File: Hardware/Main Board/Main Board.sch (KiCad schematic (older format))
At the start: 48 parts, among them Q1 NPN, Q2 NPN, Q3 A04484, SW1 Momentary, U1 MT3608, U2 NCP718A, U3 ATtiny814-SS

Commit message: added footprints to schematic. Some still need to be made but mostly all are done
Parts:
- removed MK1: MIC, symbol Device:Microphone
- added C7: .1uf, Capacitor_SMD:C_0603_1608Metric, symbol Device:C_Small
- added TP10: B-, TestPoint:TestPoint_THTPad_3.0x3.0mm_Drill1.5mm, symbol Connector:TestPoint
- added TP11: Battery-, TestPoint:TestPoint_Pad_3.0x3.0mm, symbol Connector:TestPoint
- added TP12: P+, TestPoint:TestPoint_THTPad_3.0x3.0mm_Drill1.5mm, symbol Connector:TestPoint
- added TP13: P-, TestPoint:TestPoint_THTPad_3.0x3.0mm_Drill1.5mm, symbol Connector:TestPoint
- added TP14: MIC+, TestPoint:TestPoint_Keystone_5019_Minature, symbol Connector:TestPoint
- added TP15: MIC-, TestPoint:TestPoint_Keystone_5019_Minature, symbol Connector:TestPoint
- added TP6: 3V, TestPoint:TestPoint_Pad_D2.0mm, symbol Connector:TestPoint
- added TP7: Battery+, TestPoint:TestPoint_Pad_3.0x3.0mm, symbol Connector:TestPoint
- added TP8: MIC, TestPoint:TestPoint_Pad_D2.0mm, symbol Connector:TestPoint
- added TP9: B+, TestPoint:TestPoint_THTPad_3.0x3.0mm_Drill1.5mm, symbol Connector:TestPoint
- C1, C2, C3, C5, C6: footprint (none) -> Capacitor_SMD:C_Elec_4x5.4
- C10, C11, C12, C4, C8, C9: footprint (none) -> Capacitor_SMD:C_0603_1608Metric
- D1, D2, D3: footprint (none) -> Diode_SMD:D_SOD-323
- FB1: value ? -> ACML-0805-190-T; footprint (none) -> Resistor_SMD:R_0805_2012Metric
- L1: footprint (none) -> Inductor_SMD:L_Abracon_ASPI-3012S
- L2: footprint (none) -> Inductor_SMD:L_0805_2012Metric
- Q1, Q2: value NPN -> MMBT3904-TP; footprint (none) -> Package_TO_SOT_SMD:SOT-23
- R1, R12, R13, R14, R15, R16, R17, R18, R19, R2, R20, R3, R4, R5, R6, R7, R8: footprint (none) -> Resistor_SMD:R_0603_1608Metric
- SW1: footprint (none) -> Footprints:tactile
- TH1: footprint (none) -> Capacitor_SMD:C_0805_2012Metric
- TP1, TP2: footprint (none) -> TestPoint:TestPoint_Pad_3.0x3.0mm
- TP3, TP5: footprint (none) -> TestPoint:TestPoint_Pad_D2.5mm
- TP4: footprint (none) -> TestPoint:TestPoint_Pad_D2.5m
- U1: footprint (none) -> Package_TO_SOT_SMD:SOT-23-6
- U3: value ATtiny814-SS -> ATtiny1614; symbol MCU_Microchip_ATtiny:ATtiny814-SS -> Main-Board-rescue:ATtiny814-SS-MCU_Microchip_ATtiny
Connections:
- net labels added: +3.3V, GNDREF
- net labels removed: Pack_Sense, Temp_Sense
- wire segments 116 -> 134
- no-connect marks 1 -> 6
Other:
- note added: "Battery into PCB\n"
- note added: "Charger Module"
- note added: "Design Requirements:\n\nR15 & R16 Close to U1. Feedback line short as possible. Short and wide traces\n\nC8 & C9 close to U2\n\nC10 & C11 close to U3\n\nC6 as close to pre amp as possible\n\n"
- note added: "OPTIONAL\n"
- note added: "Pins from charger to PCB"
- note added: "Pins to charger\n"
- note added: "Regulated power going here\n"
- note removed: "Design Requirements:\n\nR15 & R16 Close to U1. Feedback line short as possible. Short and wide traces\n\nC8 & C9 close to U2\n\nC10 & C11 close to U3\n\nC6 as close to pre amp supply as possible\n\n"
- moved on the sheet: TP3

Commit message: added a few more footprints before I got drunk and forgot to push lol
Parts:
- L1: footprint Inductor_SMD:L_Abracon_ASPI-3012S -> Inductor_SMD:L_Bourns_SRN6045TA
- Q3: footprint Package_TO_SOT_SMD:TDSON-8-1 -> Package_SO:SOIC-8_3.9x4.9mm_P1.27mm
- SW1: footprint Footprints:tactile -> Button_Switch_SMD:SW_SPST_PTS645
- TP4: footprint TestPoint:TestPoint_Pad_D2.5m -> TestPoint:TestPoint_Pad_D2.5mm
- U2: footprint Footprints:SON65P200X200X80-7N -> Main Board:wdfn; symbol Regulator_Linear:AP2204K-ADJ -> Main-Board-rescue:AP2127K-ADJ
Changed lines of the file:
@@
 F 0 "SW1" H 1065 6565 50  0000 C CNN
 F 1 "Momentary" H 1065 6495 50  0000 C CNN
-F 2 "Footprints:tactile" H 1085 6555 50  0001 C CNN
+F 2 "Button_Switch_SMD:SW_SPST_PTS645" H 1085 6555 50  0001 C CNN
 F 3 "~" H 1085 6555 50  0001 C CNN
 	1    1085 6355
@@
 F 0 "Q3" V 4994 6425 50  0000 C CNN
 F 1 "A04484" V 5085 6425 50  0000 C CNN
-F 2 "Package_TO_SOT_SMD:TDSON-8-1" H 4945 6350 50  0001 L CIN
+F 2 "Package_SO:SOIC-8_3.9x4.9mm_P1.27mm" H 4945 6350 50  0001 L CIN
 F 3 "http://www.ti.com/lit/gpn/csd16342q5a" V 4745 6425 50  0001 L CNN
 	1    4745 6425
@@
 F 0 "L1" V 1770 2580 50  0000 C CNN
 F 1 "10uh" V 1679 2580 50  0000 C CNN
-F 2 "Inductor_SMD:L_Abracon_ASPI-3012S" H 1545 2580 50  0001 C CNN
+F 2 "Inductor_SMD:L_Bourns_SRN6045TA" H 1545 2580 50  0001 C CNN
 F 3 "~" H 1545 2580 50  0001 C CNN
 	1    1545 2580
@@
 F 0 "TP4" V 5300 5100 50  0000 C CNN
 F 1 "GND" V 5310 4895 50  0000 C CNN
-F 2 "TestPoint:TestPoint_Pad_D2.5m" H 5510 4645 50  0001 C CNN
+F 2 "TestPoint:TestPoint_Pad_D2.5mm" H 5510 4645 50  0001 C CNN
 F 3 "~" H 5510 4645 50  0001 C CNN
 	1    5310 4645
@@
 	4774 2580 4805 2580
 $Comp
-L Regulator_Linear:AP2204K-ADJ U2
+L Main-Board-rescue:AP2127K-ADJ U2
 U 1 1 5EC19F82
 P 4362 2680
 F 0 "U2" H 4242 2985 50  0000 C CNN
 F 1 "NCP718A" H 4357 2910 50  0000 C CNN
-F 2 "Footprints:SON65P200X200X80-7N" H 4362 3005 50  0001 C CNN
+F 2 "Main Board:wdfn" H 4362 3005 50  0001 C CNN
 F 3 "https://www.onsemi.com/pub/Collateral/NCP718-D.PDF" H 4362 2780 50  0001 C CNN
 	1    4362 2680
@@
 L Connector:TestPoint TP3
 U 1 1 5EEBD8E0
-P 5320 4530
-F 0 "TP3" V 5315 4985 50  0000 C CNN
-F 1 "UDPI" V 5315 4795 50  0000 C CNN
-F 2 "TestPoint:TestPoint_Pad_D2.5mm" H 5520 4530 50  0001 C CNN
-F 3 "~" H 5520 4530 50  0001 C CNN
-	1    5320 4530
+P 5310 4530
+F 0 "TP3" V 5305 4985 50  0000 C CNN
+F 1 "UDPI" V 5305 4795 50  0000 C CNN
+F 2 "TestPoint:TestPoint_Pad_D2.5mm" H 5510 4530 50  0001 C CNN
+F 3 "~" H 5510 4530 50  0001 C CNN
+	1    5310 4530
 	0    -1   -1   0
 $EndComp
 Wire Wire Line
-	5320 4530 5510 4530
-Text Label 5510 4530 2    50   ~ 0
+	5310 4530 5500 4530
+Text Label 5500 4530 2    50   ~ 0
 PRGM
 NoConn ~ 1388 2844

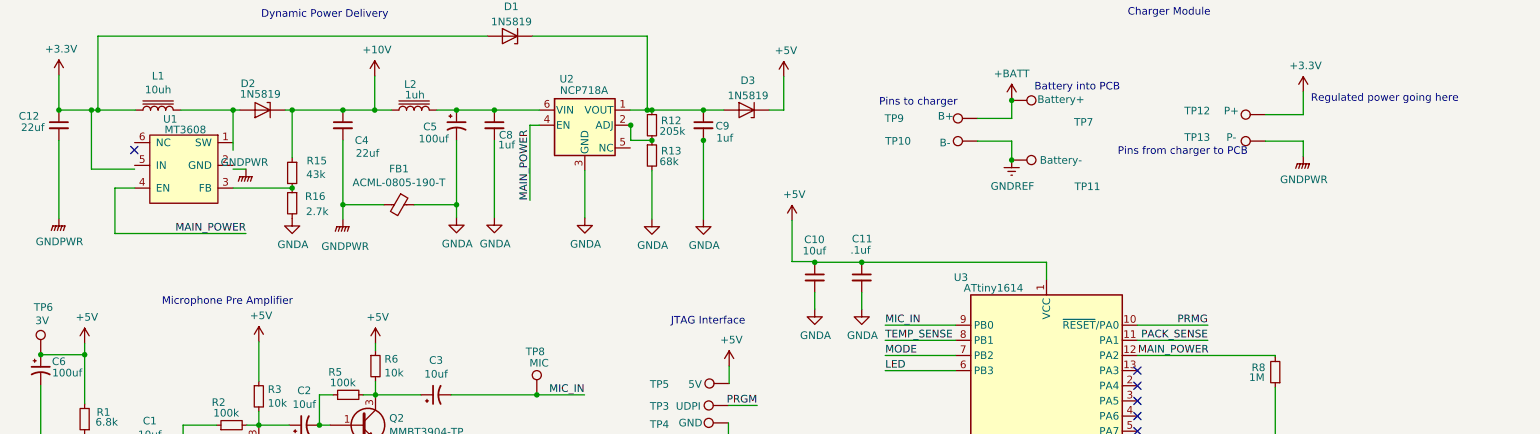
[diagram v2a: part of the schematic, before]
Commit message: placed PCB
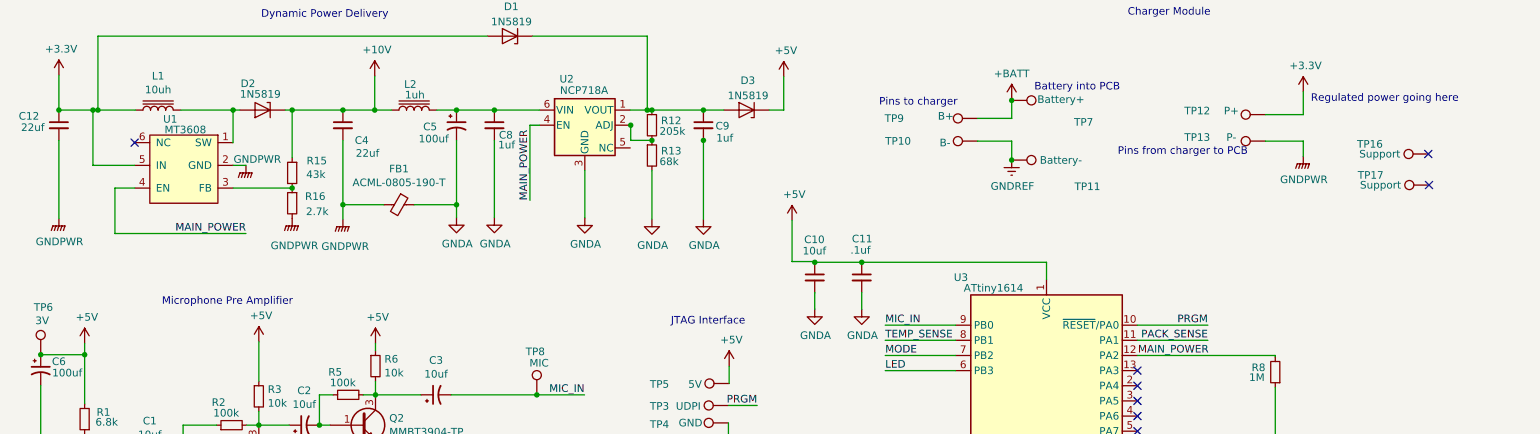
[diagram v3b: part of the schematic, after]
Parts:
- added TP16, TP17: Support, TestPoint:TestPoint_THTPad_2.0x2.0mm_Drill1.0mm, symbol Connector:TestPoint
- TP10, TP12, TP13, TP9: footprint TestPoint:TestPoint_THTPad_3.0x3.0mm_Drill1.5mm -> TestPoint:TestPoint_THTPad_2.0x2.0mm_Drill1.0mm
- U2: footprint Main Board:wdfn -> Footprints:SON65P200X200X80-7N
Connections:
- net labels removed: PRMG
- no-connect marks 6 -> 8

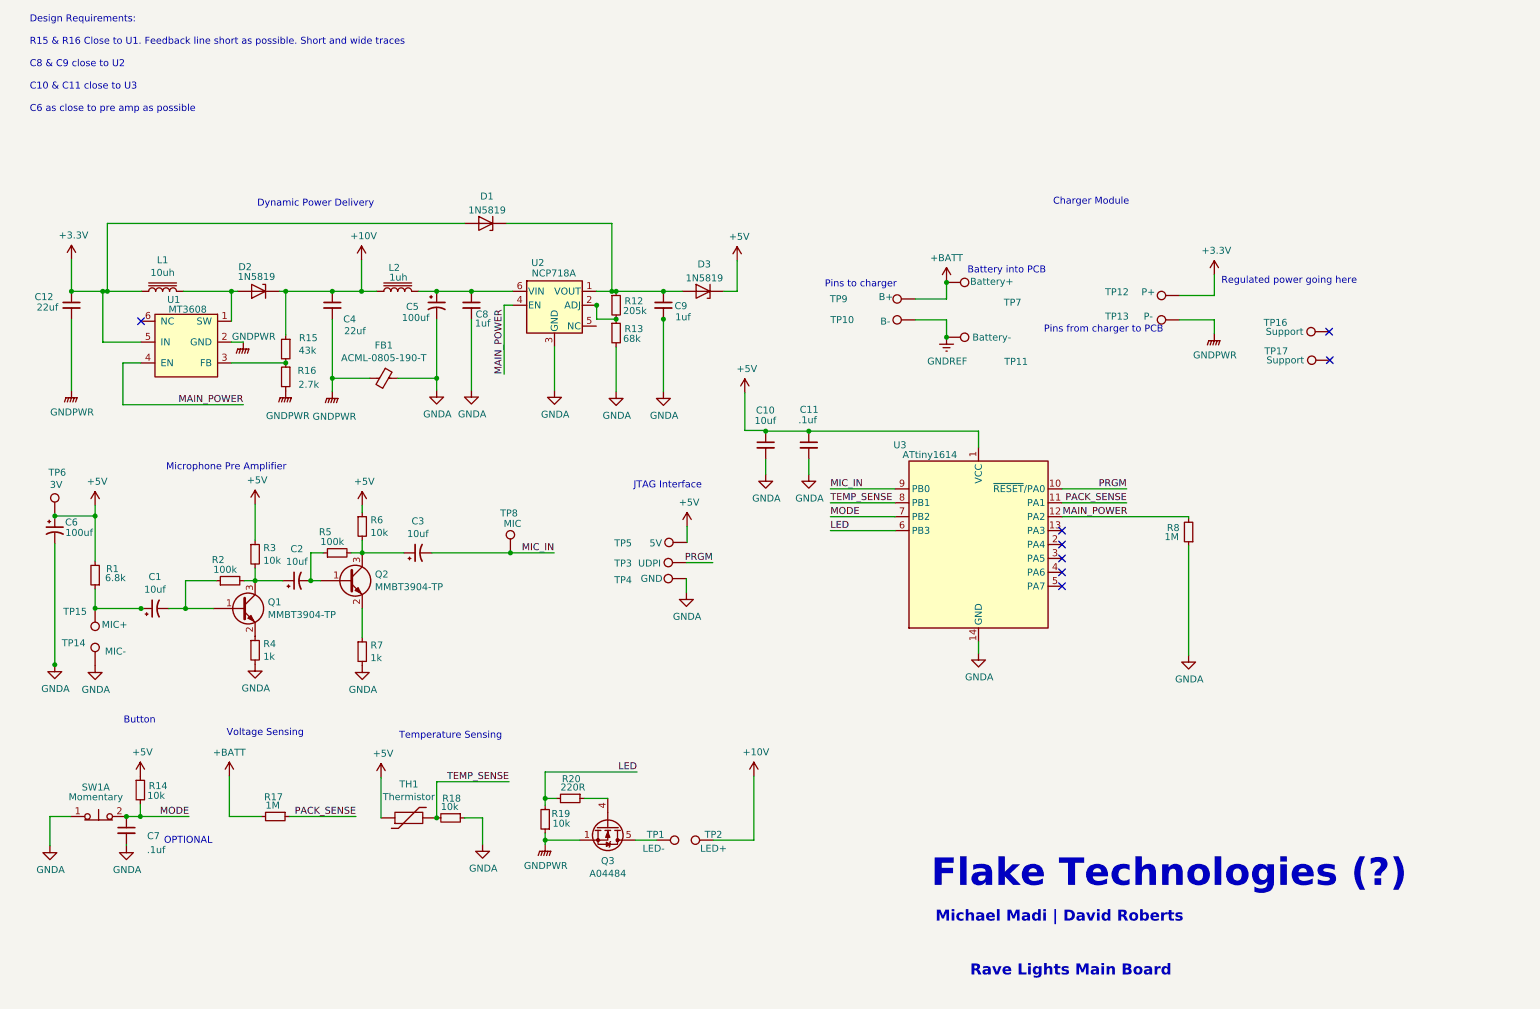
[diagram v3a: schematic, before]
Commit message: coper fills on PCB
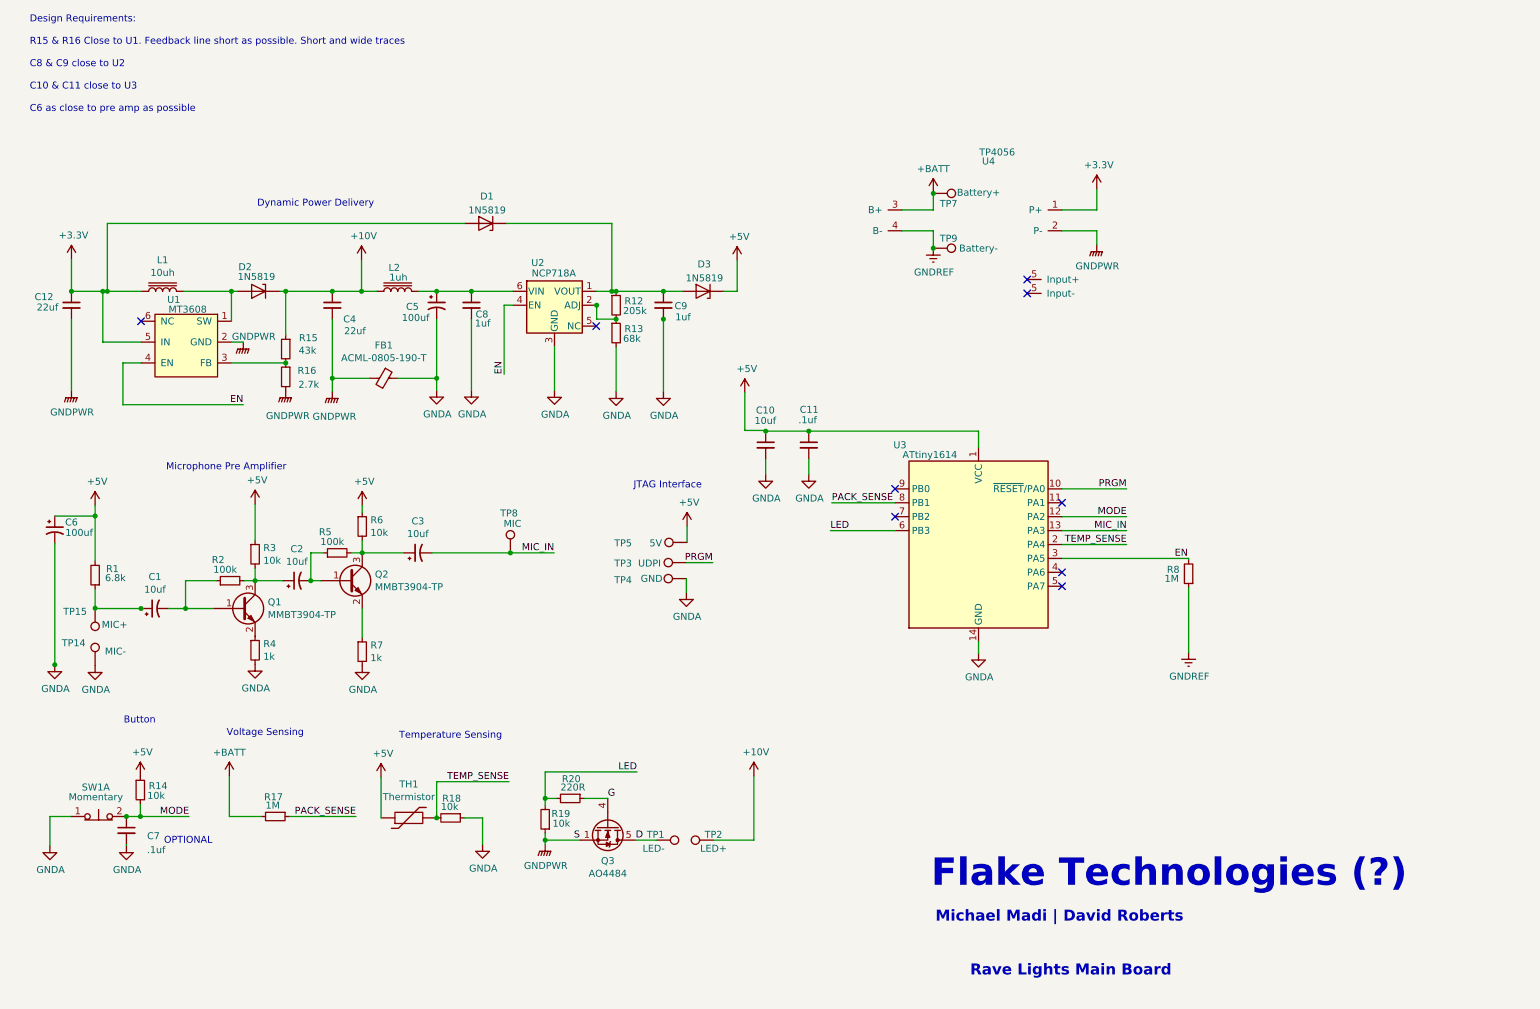
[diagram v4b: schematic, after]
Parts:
- removed TP10: B-, TestPoint:TestPoint_THTPad_2.0x2.0mm_Drill1.0mm, symbol Connector:TestPoint
- removed TP11: Battery-, TestPoint:TestPoint_Pad_3.0x3.0mm, symbol Connector:TestPoint
- removed TP12: P+, TestPoint:TestPoint_THTPad_2.0x2.0mm_Drill1.0mm, symbol Connector:TestPoint
- removed TP13: P-, TestPoint:TestPoint_THTPad_2.0x2.0mm_Drill1.0mm, symbol Connector:TestPoint
- removed TP16, TP17: Support, TestPoint:TestPoint_THTPad_2.0x2.0mm_Drill1.0mm, symbol Connector:TestPoint
- removed TP6: 3V, TestPoint:TestPoint_Pad_D2.0mm, symbol Connector:TestPoint
- added U4: TP4056, Main Board1:charger, symbol Main-Board-rescue:TP4056
- Q3: value A04484 -> AO4484; footprint Package_SO:SOIC-8_3.9x4.9mm_P1.27mm -> Main Board1:SOIC-8_3.9x4.9mm_P1.27mm
- TP9: value B+ -> Battery-; footprint TestPoint:TestPoint_THTPad_2.0x2.0mm_Drill1.0mm -> TestPoint:TestPoint_Pad_3.0x3.0mm
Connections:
- net labels added: D, EN, G, S
- net labels removed: MAIN_POWER
- no-connect marks 8 -> 9
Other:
- note removed: "Battery into PCB\n"
- note removed: "Charger Module"
- note removed: "Pins from charger to PCB"
- note removed: "Pins to charger\n"
- note removed: "Regulated power going here\n"
- moved on the sheet: R8

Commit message: PCB fixeruppers
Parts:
- C1, C2, C3: footprint Capacitor_SMD:C_Elec_4x5.4 -> Main Board:CP_Elec_4x3
- C5, C6: footprint Capacitor_SMD:C_Elec_4x5.4 -> Main Board:100
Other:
- note added: "Flake Technologies\n\n"
- note added: "Michael Madi | David Roberts | www.flaketechnologies.ca\n"
- note removed: "Flake Technologies (?)\n"
- note removed: "Michael Madi | David Roberts\n\n"
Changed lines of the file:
@@
 EESchema Schematic File Version 4
+LIBS:Main Board-cache
 EELAYER 30 0
 EELAYER END
@@
 F 0 "C3" V 3608 4460 50  0000 C CNN
 F 1 "10uf" V 3517 4460 50  0000 C CNN
-F 2 "Capacitor_SMD:C_Elec_4x5.4" H 3380 4460 50  0001 C CNN
+F 2 "Main Board:CP_Elec_4x3" H 3380 4460 50  0001 C CNN
 F 3 "~" H 3380 4460 50  0001 C CNN
 	1    3380 4460
@@
 F 0 "C2" V 2738 4660 50  0000 C CNN
 F 1 "10uf" V 2647 4660 50  0000 C CNN
-F 2 "Capacitor_SMD:C_Elec_4x5.4" H 2510 4660 50  0001 C CNN
+F 2 "Main Board:CP_Elec_4x3" H 2510 4660 50  0001 C CNN
 F 3 "~" H 2510 4660 50  0001 C CNN
 	1    2510 4660
@@
 F 0 "C5" H 3295 2670 50  0000 L CNN
 F 1 "100uf" H 3265 2590 50  0000 L CNN
-F 2 "Capacitor_SMD:C_Elec_4x5.4" H 3515 2680 50  0001 C CNN
+F 2 "Main Board:100" H 3515 2680 50  0001 C CNN
 F 3 "~" H 3515 2680 50  0001 C CNN
 	1    3515 2680
@@
 	1    0    0    -1
 $EndComp
-Text Notes 7070 6880 0    197  ~ 39
-Flake Technologies (?)\n
-Text Notes 7100 7250 0    79   ~ 16
-Michael Madi | David Roberts\n\n
+Text Notes 7030 7110 0    79   ~ 16
+Michael Madi | David Roberts | www.flaketechnologies.ca\n
 Text Notes 7350 7510 0    79   ~ 16
 Rave Lights Main Board\n
@@
 F 0 "C6" H 890 4350 50  0000 C CNN
 F 1 "100uf" H 945 4275 50  0000 C CNN
-F 2 "Capacitor_SMD:C_Elec_4x5.4" H 770 4295 50  0001 C CNN
+F 2 "Main Board:100" H 770 4295 50  0001 C CNN
 F 3 "~" H 770 4295 50  0001 C CNN
 	1    770  4295
@@
 F 0 "C1" V 1718 4860 50  0000 C CNN
 F 1 "10uf" V 1627 4860 50  0000 C CNN
-F 2 "Capacitor_SMD:C_Elec_4x5.4" H 1490 4860 50  0001 C CNN
+F 2 "Main Board:CP_Elec_4x3" H 1490 4860 50  0001 C CNN
 F 3 "~" H 1490 4860 50  0001 C CNN
 	1    1490 4860
@@
 Text Label 5500 4530 2    50   ~ 0
 PRGM
-Text Notes 590  1380 0    50   ~ 0
+Text Notes 2870 1560 0    50   ~ 0
 Design Requirements:\n\nR15 & R16 Close to U1. Feedback line short as possible. Short and wide traces\n\nC8 & C9 close to U2\n\nC10 & C11 close to U3\n\nC6 as close to pre amp as possible\n\n
 $Comp
@@
 NoConn ~ 6810 4200
 $Comp
-L power:GNDREF #PWR?
+L power:GNDREF #PWR0104
 U 1 1 5F063991
 P 8920 5175
-F 0 "#PWR?" H 8920 4925 50  0001 C CNN
+F 0 "#PWR0104" H 8920 4925 50  0001 C CNN
 F 1 "GNDREF" H 8925 5002 50  0000 C CNN
 F 2 "" H 8920 5175 50  0001 C CNN
@@
 	1    0    0    -1
 $EndComp
+Text Notes 7080 7260 0    197  ~ 39
+Flake Technologies\n\n
+$Comp
+L Main-Board-rescue:LOGO #G1
+U 1 1 5F13D2FC
+P 6160 7300
+F 0 "#G1" H 6160 6833 60  0001 C CNN
+F 1 "LOGO" H 6160 7767 60  0001 C CNN
+F 2 "" H 6160 7300 50  0001 C CNN
+F 3 "" H 6160 7300 50  0001 C CNN
+	1    6160 7300
+	1    0    0    -1
+$EndComp

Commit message: added marketing folder. we should maybe make a G drive soon if we start filling up.
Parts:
- L1: footprint Inductor_SMD:L_Bourns_SRN6045TA -> Main Board:BW10uHInductor
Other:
- moved on the sheet: R8
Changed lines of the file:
@@
 F 0 "L1" V 1770 2580 50  0000 C CNN
 F 1 "10uh" V 1679 2580 50  0000 C CNN
-F 2 "Inductor_SMD:L_Bourns_SRN6045TA" H 1545 2580 50  0001 C CNN
+F 2 "Main Board:BW10uHInductor" H 1545 2580 50  0001 C CNN
 F 3 "~" H 1545 2580 50  0001 C CNN
 	1    1545 2580
@@
 Text Label 8475 4300 2    50   ~ 0
 MIC_IN
-Text Label 8475 4400 2    50   ~ 0
+Text Label 8475 4600 2    50   ~ 0
 TEMP_SENSE
 Wire Wire Line
-	8475 4400 8010 4400
+	8475 4600 8010 4600
 Wire Wire Line
 	6345 4300 6810 4300
@@
 	8475 4300 8010 4300
 Wire Wire Line
-	8010 4200 8475 4200
-Text Label 8475 4200 2    50   ~ 0
-MODE
-Text Label 8915 4500 2    50   ~ 0
+	8010 4500 8475 4500
+Text Label 8915 4700 2    50   ~ 0
 EN
 Wire Wire Line
@@
 L Device:R_Small R8
 U 1 1 5F2B9B1E
-P 8920 4610
-F 0 "R8" H 8985 4580 50  0000 L CNN
-F 1 "1M" H 8990 4645 50  0000 L CNN
-F 2 "Resistor_SMD:R_0603_1608Metric" H 8920 4610 50  0001 C CNN
-F 3 "~" H 8920 4610 50  0001 C CNN
-	1    8920 4610
+P 8920 4810
+F 0 "R8" H 8985 4780 50  0000 L CNN
+F 1 "1M" H 8990 4845 50  0000 L CNN
+F 2 "Resistor_SMD:R_0603_1608Metric" H 8920 4810 50  0001 C CNN
+F 3 "~" H 8920 4810 50  0001 C CNN
+	1    8920 4810
 	-1   0    0    1
 $EndComp
 Wire Wire Line
-	8920 4500 8920 4510
-Wire Wire Line
-	8010 4500 8920 4500
+	8920 4700 8920 4710
+Wire Wire Line
+	8010 4700 8920 4700
 $Comp
 L power:GNDA #PWR025
@@
 Text Notes 1555 6560 0    50   ~ 0
 OPTIONAL\n
-NoConn ~ 8010 4700
 Wire Wire Line
 	4362 2980 4362 3292
@@
 Text Label 5500 4530 2    50   ~ 0
 PRGM
-Text Notes 2870 1560 0    50   ~ 0
+Text Notes 740  1460 0    50   ~ 0
 Design Requirements:\n\nR15 & R16 Close to U1. Feedback line short as possible. Short and wide traces\n\nC8 & C9 close to U2\n\nC10 & C11 close to U3\n\nC6 as close to pre amp as possible\n\n
 $Comp
@@
 NoConn ~ 7760 2595
 Wire Wire Line
-	8920 4710 8920 5175
+	8920 4910 8920 5375
 NoConn ~ 6810 4000
 NoConn ~ 8010 4100
 Wire Wire Line
 	6810 4100 6355 4100
-NoConn ~ 8010 4600
 NoConn ~ 6810 4200
 $Comp
 L power:GNDREF #PWR0104
 U 1 1 5F063991
-P 8920 5175
-F 0 "#PWR0104" H 8920 4925 50  0001 C CNN
-F 1 "GNDREF" H 8925 5002 50  0000 C CNN
-F 2 "" H 8920 5175 50  0001 C CNN
-F 3 "" H 8920 5175 50  0001 C CNN
-	1    8920 5175
+P 8920 5375
+F 0 "#PWR0104" H 8920 5125 50  0001 C CNN
+F 1 "GNDREF" H 8925 5202 50  0000 C CNN
+F 2 "" H 8920 5375 50  0001 C CNN
+F 3 "" H 8920 5375 50  0001 C CNN
+	1    8920 5375
 	1    0    0    -1
 $EndComp
@@
 	1    0    0    -1
 $EndComp
+Text Label 8475 4500 2    50   ~ 0
+MODE
+NoConn ~ 8010 4200
+NoConn ~ 8010 4400
 $EndSCHEMATC
